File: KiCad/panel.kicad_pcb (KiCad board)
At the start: 2 copper layers, 50 x 50 mm, 38 parts, among them J1 Conn_01x05, J5 USB_C_Receptacle_USB2.0_16P, J6 Conn_01x03, J7 VDD, J8 GND, J9 Conn_01x14, Q1 IRLZ44N, Q2 IRLZ44N, Q3 IRLZ44N, Q4 IRLZ44N, SW1 BOOT, SW2 ENABLE, U1 TPS62132, U2 ESP32-S3-WROOM-2

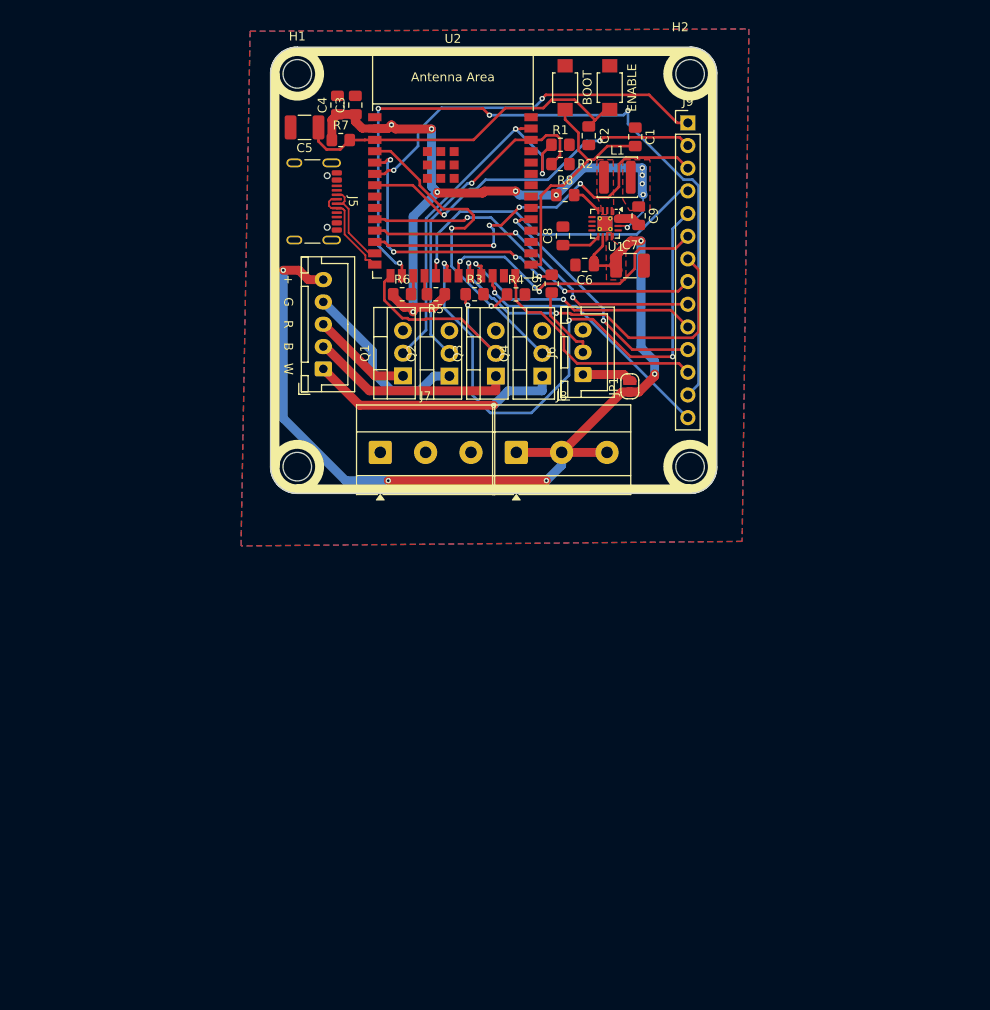
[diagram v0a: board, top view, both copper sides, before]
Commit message: convert to 4 layer pcb
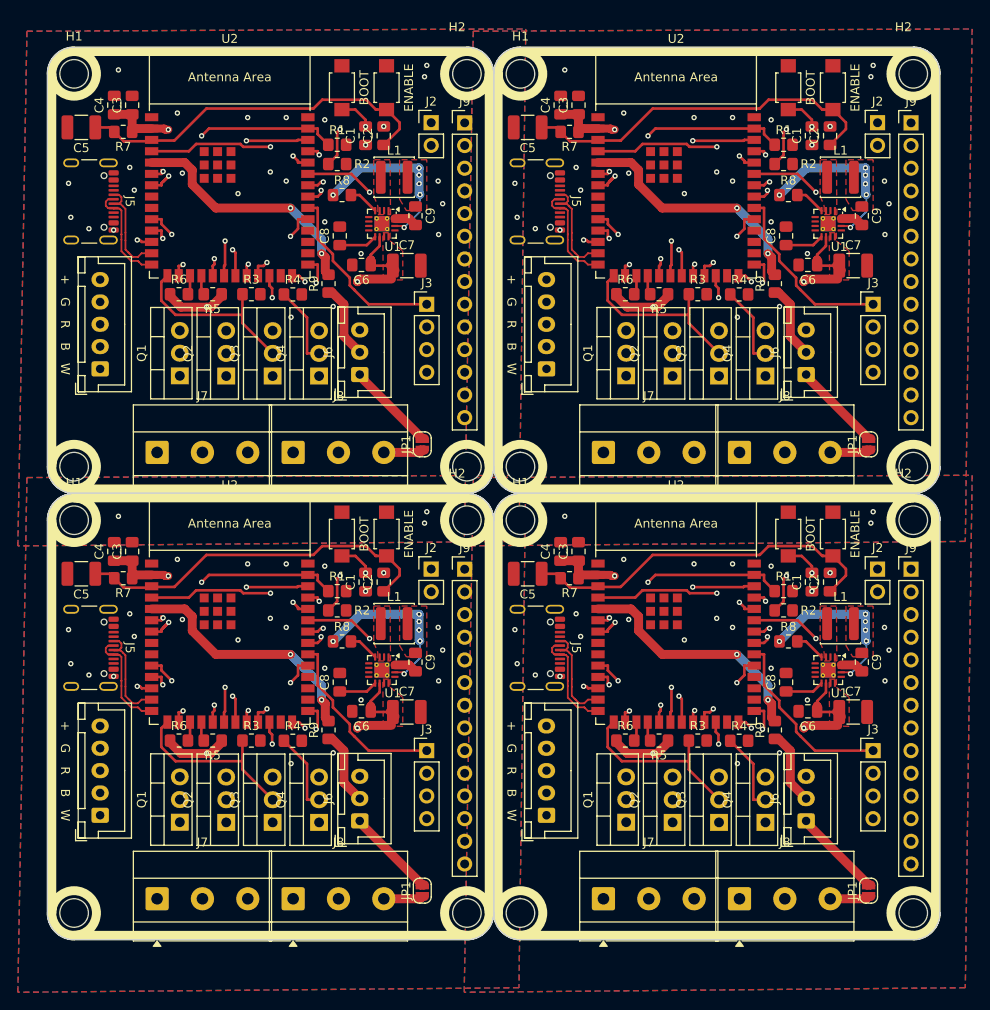
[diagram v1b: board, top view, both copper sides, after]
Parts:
- removed the C1 at (164.4, 30.1)
- removed the C2 at (159.2, 29.9)
- removed the C3 at (133.0, 26.5)
- removed the C4 at (131.0, 26.5)
- removed the C5 at (127.3, 29.0)
- removed the C6 at (158.7, 44.4)
- removed the C7 at (163.8, 44.5)
- removed the C8 at (156.3, 41.1)
- removed the C9 at (164.7, 38.9)
- removed the H1 at (126.5, 23.0)
- removed the H2 at (170.5, 23.0)
- removed the H3 at (170.5, 67.0)
- removed the H4 at (126.5, 67.0)
- removed the J1 at (129.4, 56.0)
- removed the J5 at (127.2, 37.3)
- removed the J6 at (158.5, 56.7)
- removed the J7 at (135.8, 65.4)
- removed the J8 at (151.0, 65.4)
- removed the J9 at (170.2, 28.5)
- removed the JP1 at (163.8, 58.0)
- removed the L1 at (162.4, 34.6)
- removed the Q1 at (138.3, 56.8)
- removed the Q2 at (143.5, 56.9)
- removed the Q3 at (148.7, 56.9)
- removed the Q4 at (153.9, 56.9)
- removed the R1 at (156.0, 30.9)
- removed the R2 at (156.0, 33.1)
- removed the R3 at (146.4, 47.7)
- removed the R4 at (151.0, 47.7)
- removed the R5 at (142.0, 47.7)
- removed the R6 at (138.2, 47.7)
- removed the R7 at (131.4, 30.4)
- removed the R8 at (156.5, 36.6)
- removed the R9 at (155.0, 46.5)
- removed the SW1 at (156.5, 24.6)
- removed the SW2 at (161.5, 24.6)
- removed the U1 at (161.0, 39.8)
- removed the U2 at (143.9, 36.1)
- added C1: 100n, Capacitor_SMD:C_0805_2012Metric_Pad1.18x1.45mm_HandSolder, F.Cu at (184.2, 29.9)
- added C1: 100n, Capacitor_SMD:C_0805_2012Metric_Pad1.18x1.45mm_HandSolder, F.Cu at (134.2, 29.9)
- added C1: 100n, Capacitor_SMD:C_0805_2012Metric_Pad1.18x1.45mm_HandSolder, F.Cu at (134.2, 79.9)
- added C1: 100n, Capacitor_SMD:C_0805_2012Metric_Pad1.18x1.45mm_HandSolder, F.Cu at (184.2, 79.9)
- added C2: 100n, Capacitor_SMD:C_0805_2012Metric_Pad1.18x1.45mm_HandSolder, F.Cu at (136.2, 79.9)
- added C2: 100n, Capacitor_SMD:C_0805_2012Metric_Pad1.18x1.45mm_HandSolder, F.Cu at (136.2, 29.9)
- added C2: 100n, Capacitor_SMD:C_0805_2012Metric_Pad1.18x1.45mm_HandSolder, F.Cu at (186.2, 79.9)
- added C2: 100n, Capacitor_SMD:C_0805_2012Metric_Pad1.18x1.45mm_HandSolder, F.Cu at (186.2, 29.9)
- added C3: 100n, Capacitor_SMD:C_0805_2012Metric_Pad1.18x1.45mm_HandSolder, F.Cu at (108.0, 76.5)
- added C3: 100n, Capacitor_SMD:C_0805_2012Metric_Pad1.18x1.45mm_HandSolder, F.Cu at (158.0, 76.5)
- added C3: 100n, Capacitor_SMD:C_0805_2012Metric_Pad1.18x1.45mm_HandSolder, F.Cu at (108.0, 26.5)
- added C3: 100n, Capacitor_SMD:C_0805_2012Metric_Pad1.18x1.45mm_HandSolder, F.Cu at (158.0, 26.5)
- added C4: 22u, Capacitor_SMD:C_0805_2012Metric_Pad1.18x1.45mm_HandSolder, F.Cu at (156.0, 76.5)
- added C4: 22u, Capacitor_SMD:C_0805_2012Metric_Pad1.18x1.45mm_HandSolder, F.Cu at (156.0, 26.5)
- added C4: 22u, Capacitor_SMD:C_0805_2012Metric_Pad1.18x1.45mm_HandSolder, F.Cu at (106.0, 26.5)
- added C4: 22u, Capacitor_SMD:C_0805_2012Metric_Pad1.18x1.45mm_HandSolder, F.Cu at (106.0, 76.5)
- added C5: 10u, Capacitor_SMD:C_1210_3225Metric_Pad1.33x2.70mm_HandSolder, F.Cu at (152.3, 29.0)
- added C5: 10u, Capacitor_SMD:C_1210_3225Metric_Pad1.33x2.70mm_HandSolder, F.Cu at (102.3, 29.0)
- added C5: 10u, Capacitor_SMD:C_1210_3225Metric_Pad1.33x2.70mm_HandSolder, F.Cu at (102.3, 79.0)
- added C5: 10u, Capacitor_SMD:C_1210_3225Metric_Pad1.33x2.70mm_HandSolder, F.Cu at (152.3, 79.0)
- added C6: 100n, Capacitor_SMD:C_0805_2012Metric_Pad1.18x1.45mm_HandSolder, F.Cu at (183.7, 44.4)
- added C6: 100n, Capacitor_SMD:C_0805_2012Metric_Pad1.18x1.45mm_HandSolder, F.Cu at (133.7, 94.4)
- added C6: 100n, Capacitor_SMD:C_0805_2012Metric_Pad1.18x1.45mm_HandSolder, F.Cu at (183.7, 94.4)
- added C6: 100n, Capacitor_SMD:C_0805_2012Metric_Pad1.18x1.45mm_HandSolder, F.Cu at (133.7, 44.4)
- added C7: 10u, Capacitor_SMD:C_1210_3225Metric_Pad1.33x2.70mm_HandSolder, F.Cu at (138.8, 94.5)
- added C7: 10u, Capacitor_SMD:C_1210_3225Metric_Pad1.33x2.70mm_HandSolder, F.Cu at (188.8, 94.5)
- added C7: 10u, Capacitor_SMD:C_1210_3225Metric_Pad1.33x2.70mm_HandSolder, F.Cu at (188.8, 44.5)
- added C7: 10u, Capacitor_SMD:C_1210_3225Metric_Pad1.33x2.70mm_HandSolder, F.Cu at (138.8, 44.5)
- added C8: 3.3n, Capacitor_SMD:C_0805_2012Metric_Pad1.18x1.45mm_HandSolder, F.Cu at (131.3, 91.1)
- added C8: 3.3n, Capacitor_SMD:C_0805_2012Metric_Pad1.18x1.45mm_HandSolder, F.Cu at (181.3, 41.1)
- added C8: 3.3n, Capacitor_SMD:C_0805_2012Metric_Pad1.18x1.45mm_HandSolder, F.Cu at (181.3, 91.1)
- added C8: 3.3n, Capacitor_SMD:C_0805_2012Metric_Pad1.18x1.45mm_HandSolder, F.Cu at (131.3, 41.1)
- added C9: 22u, Capacitor_SMD:C_0805_2012Metric_Pad1.18x1.45mm_HandSolder, F.Cu at (189.7, 38.9)
- added C9: 22u, Capacitor_SMD:C_0805_2012Metric_Pad1.18x1.45mm_HandSolder, F.Cu at (139.7, 88.9)
- added C9: 22u, Capacitor_SMD:C_0805_2012Metric_Pad1.18x1.45mm_HandSolder, F.Cu at (189.7, 88.9)
- added C9: 22u, Capacitor_SMD:C_0805_2012Metric_Pad1.18x1.45mm_HandSolder, F.Cu at (139.7, 38.9)
- added H1: MountingHole, MountingHole:MountingHole_3.2mm_M3, F.Cu at (151.5, 23.0)
- added H1: MountingHole, MountingHole:MountingHole_3.2mm_M3, F.Cu at (101.5, 23.0)
- added H1: MountingHole, MountingHole:MountingHole_3.2mm_M3, F.Cu at (101.5, 73.0)
- added H1: MountingHole, MountingHole:MountingHole_3.2mm_M3, F.Cu at (151.5, 73.0)
- added H2: MountingHole, MountingHole:MountingHole_3.2mm_M3, F.Cu at (145.5, 23.0)
- added H2: MountingHole, MountingHole:MountingHole_3.2mm_M3, F.Cu at (195.5, 23.0)
- added H2: MountingHole, MountingHole:MountingHole_3.2mm_M3, F.Cu at (195.5, 73.0)
- added H2: MountingHole, MountingHole:MountingHole_3.2mm_M3, F.Cu at (145.5, 73.0)
- added H3: MountingHole, MountingHole:MountingHole_3.2mm_M3, F.Cu at (145.5, 117.0)
- added H3: MountingHole, MountingHole:MountingHole_3.2mm_M3, F.Cu at (195.5, 67.0)
- added H3: MountingHole, MountingHole:MountingHole_3.2mm_M3, F.Cu at (195.5, 117.0)
- added H3: MountingHole, MountingHole:MountingHole_3.2mm_M3, F.Cu at (145.5, 67.0)
- added H4: MountingHole, MountingHole:MountingHole_3.2mm_M3, F.Cu at (101.5, 117.0)
- added H4: MountingHole, MountingHole:MountingHole_3.2mm_M3, F.Cu at (101.5, 67.0)
- added H4: MountingHole, MountingHole:MountingHole_3.2mm_M3, F.Cu at (151.5, 67.0)
- added H4: MountingHole, MountingHole:MountingHole_3.2mm_M3, F.Cu at (151.5, 117.0)
- added J1: Conn_01x05, Connector_JST:JST_XH_B5B-XH-A_1x05_P2.50mm_Vertical, F.Cu at (104.4, 106.0)
- added J1: Conn_01x05, Connector_JST:JST_XH_B5B-XH-A_1x05_P2.50mm_Vertical, F.Cu at (154.4, 106.0)
- added J1: Conn_01x05, Connector_JST:JST_XH_B5B-XH-A_1x05_P2.50mm_Vertical, F.Cu at (154.4, 56.0)
- added J1: Conn_01x05, Connector_JST:JST_XH_B5B-XH-A_1x05_P2.50mm_Vertical, F.Cu at (104.4, 56.0)
- added J2: UART, Connector_PinHeader_2.54mm:PinHeader_1x02_P2.54mm_Vertical, F.Cu at (191.5, 78.5)
- added J2: UART, Connector_PinHeader_2.54mm:PinHeader_1x02_P2.54mm_Vertical, F.Cu at (141.5, 28.5)
- added J2: UART, Connector_PinHeader_2.54mm:PinHeader_1x02_P2.54mm_Vertical, F.Cu at (191.5, 28.5)
- added J2: UART, Connector_PinHeader_2.54mm:PinHeader_1x02_P2.54mm_Vertical, F.Cu at (141.5, 78.5)
- added J3: JTAG, Connector_PinHeader_2.54mm:PinHeader_1x04_P2.54mm_Vertical, F.Cu at (141.0, 48.8)
- added J3: JTAG, Connector_PinHeader_2.54mm:PinHeader_1x04_P2.54mm_Vertical, F.Cu at (191.0, 48.8)
- added J3: JTAG, Connector_PinHeader_2.54mm:PinHeader_1x04_P2.54mm_Vertical, F.Cu at (191.0, 98.8)
- added J3: JTAG, Connector_PinHeader_2.54mm:PinHeader_1x04_P2.54mm_Vertical, F.Cu at (141.0, 98.8)
- added J5: USB_C_Receptacle_USB2.0_16P, Connector_USB:USB_C_Receptacle_GCT_USB4105-xx-A_16P_TopMnt_Horizontal, F.Cu at (102.2, 37.3)
- added J5: USB_C_Receptacle_USB2.0_16P, Connector_USB:USB_C_Receptacle_GCT_USB4105-xx-A_16P_TopMnt_Horizontal, F.Cu at (152.2, 37.3)
- added J5: USB_C_Receptacle_USB2.0_16P, Connector_USB:USB_C_Receptacle_GCT_USB4105-xx-A_16P_TopMnt_Horizontal, F.Cu at (152.2, 87.3)
- added J5: USB_C_Receptacle_USB2.0_16P, Connector_USB:USB_C_Receptacle_GCT_USB4105-xx-A_16P_TopMnt_Horizontal, F.Cu at (102.2, 87.3)
- added J6: Conn_01x03, Connector_JST:JST_XH_B3B-XH-A_1x03_P2.50mm_Vertical, F.Cu at (183.5, 106.7)
- added J6: Conn_01x03, Connector_JST:JST_XH_B3B-XH-A_1x03_P2.50mm_Vertical, F.Cu at (183.5, 56.7)
- added J6: Conn_01x03, Connector_JST:JST_XH_B3B-XH-A_1x03_P2.50mm_Vertical, F.Cu at (133.5, 106.7)
- added J6: Conn_01x03, Connector_JST:JST_XH_B3B-XH-A_1x03_P2.50mm_Vertical, F.Cu at (133.5, 56.7)
- added J7: VDD, TerminalBlock_Phoenix:TerminalBlock_Phoenix_MKDS-1,5-3-5.08_1x03_P5.08mm_Horizontal, F.Cu at (160.8, 115.4)
- added J7: VDD, TerminalBlock_Phoenix:TerminalBlock_Phoenix_MKDS-1,5-3-5.08_1x03_P5.08mm_Horizontal, F.Cu at (160.8, 65.4)
- added J7: VDD, TerminalBlock_Phoenix:TerminalBlock_Phoenix_MKDS-1,5-3-5.08_1x03_P5.08mm_Horizontal, F.Cu at (110.8, 115.4)
- added J7: VDD, TerminalBlock_Phoenix:TerminalBlock_Phoenix_MKDS-1,5-3-5.08_1x03_P5.08mm_Horizontal, F.Cu at (110.8, 65.4)
- added J8: GND, TerminalBlock_Phoenix:TerminalBlock_Phoenix_MKDS-1,5-3-5.08_1x03_P5.08mm_Horizontal, F.Cu at (126.0, 65.4)
- added J8: GND, TerminalBlock_Phoenix:TerminalBlock_Phoenix_MKDS-1,5-3-5.08_1x03_P5.08mm_Horizontal, F.Cu at (176.0, 115.4)
- added J8: GND, TerminalBlock_Phoenix:TerminalBlock_Phoenix_MKDS-1,5-3-5.08_1x03_P5.08mm_Horizontal, F.Cu at (126.0, 115.4)
- added J8: GND, TerminalBlock_Phoenix:TerminalBlock_Phoenix_MKDS-1,5-3-5.08_1x03_P5.08mm_Horizontal, F.Cu at (176.0, 65.4)
- added J9: Conn_01x14, Connector_PinHeader_2.54mm:PinHeader_1x14_P2.54mm_Vertical, F.Cu at (145.2, 78.5)
- added J9: Conn_01x14, Connector_PinHeader_2.54mm:PinHeader_1x14_P2.54mm_Vertical, F.Cu at (195.2, 28.5)
- added J9: Conn_01x14, Connector_PinHeader_2.54mm:PinHeader_1x14_P2.54mm_Vertical, F.Cu at (145.2, 28.5)
- added J9: Conn_01x14, Connector_PinHeader_2.54mm:PinHeader_1x14_P2.54mm_Vertical, F.Cu at (195.2, 78.5)
- added JP1: SolderJumper_2_Open, Jumper:SolderJumper-2_P1.3mm_Open_RoundedPad1.0x1.5mm, F.Cu at (190.5, 64.5)
- added JP1: SolderJumper_2_Open, Jumper:SolderJumper-2_P1.3mm_Open_RoundedPad1.0x1.5mm, F.Cu at (140.5, 64.5)
- added JP1: SolderJumper_2_Open, Jumper:SolderJumper-2_P1.3mm_Open_RoundedPad1.0x1.5mm, F.Cu at (140.5, 114.5)
- added JP1: SolderJumper_2_Open, Jumper:SolderJumper-2_P1.3mm_Open_RoundedPad1.0x1.5mm, F.Cu at (190.5, 114.5)
- added L1: 1/2.2u, Inductor_SMD:L_APV_ANR4026, F.Cu at (187.4, 84.6)
- added L1: 1/2.2u, Inductor_SMD:L_APV_ANR4026, F.Cu at (137.4, 84.6)
- added L1: 1/2.2u, Inductor_SMD:L_APV_ANR4026, F.Cu at (187.4, 34.6)
- added L1: 1/2.2u, Inductor_SMD:L_APV_ANR4026, F.Cu at (137.4, 34.6)
- added Q1: IRLZ44N, Package_TO_SOT_THT:TO-220-3_Vertical, F.Cu at (113.3, 106.8)
- added Q1: IRLZ44N, Package_TO_SOT_THT:TO-220-3_Vertical, F.Cu at (163.3, 106.8)
- added Q1: IRLZ44N, Package_TO_SOT_THT:TO-220-3_Vertical, F.Cu at (163.3, 56.8)
- added Q1: IRLZ44N, Package_TO_SOT_THT:TO-220-3_Vertical, F.Cu at (113.3, 56.8)
- added Q2: IRLZ44N, Package_TO_SOT_THT:TO-220-3_Vertical, F.Cu at (118.5, 106.9)
- added Q2: IRLZ44N, Package_TO_SOT_THT:TO-220-3_Vertical, F.Cu at (168.5, 56.9)
- added Q2: IRLZ44N, Package_TO_SOT_THT:TO-220-3_Vertical, F.Cu at (118.5, 56.9)
- added Q2: IRLZ44N, Package_TO_SOT_THT:TO-220-3_Vertical, F.Cu at (168.5, 106.9)
- added Q3: IRLZ44N, Package_TO_SOT_THT:TO-220-3_Vertical, F.Cu at (173.7, 56.9)
- added Q3: IRLZ44N, Package_TO_SOT_THT:TO-220-3_Vertical, F.Cu at (123.7, 56.9)
- added Q3: IRLZ44N, Package_TO_SOT_THT:TO-220-3_Vertical, F.Cu at (173.7, 106.9)
- added Q3: IRLZ44N, Package_TO_SOT_THT:TO-220-3_Vertical, F.Cu at (123.7, 106.9)
- added Q4: IRLZ44N, Package_TO_SOT_THT:TO-220-3_Vertical, F.Cu at (178.9, 106.9)
- added Q4: IRLZ44N, Package_TO_SOT_THT:TO-220-3_Vertical, F.Cu at (128.9, 56.9)
- added Q4: IRLZ44N, Package_TO_SOT_THT:TO-220-3_Vertical, F.Cu at (178.9, 56.9)
- added Q4: IRLZ44N, Package_TO_SOT_THT:TO-220-3_Vertical, F.Cu at (128.9, 106.9)
- added R1: 100k, Resistor_SMD:R_0805_2012Metric_Pad1.20x1.40mm_HandSolder, F.Cu at (181.0, 30.9)
- added R1: 100k, Resistor_SMD:R_0805_2012Metric_Pad1.20x1.40mm_HandSolder, F.Cu at (131.0, 30.9)
- added R1: 100k, Resistor_SMD:R_0805_2012Metric_Pad1.20x1.40mm_HandSolder, F.Cu at (131.0, 80.9)
- added R1: 100k, Resistor_SMD:R_0805_2012Metric_Pad1.20x1.40mm_HandSolder, F.Cu at (181.0, 80.9)
- added R2: 100k, Resistor_SMD:R_0805_2012Metric_Pad1.20x1.40mm_HandSolder, F.Cu at (181.0, 33.1)
- added R2: 100k, Resistor_SMD:R_0805_2012Metric_Pad1.20x1.40mm_HandSolder, F.Cu at (131.0, 83.1)
- added R2: 100k, Resistor_SMD:R_0805_2012Metric_Pad1.20x1.40mm_HandSolder, F.Cu at (131.0, 33.1)
- added R2: 100k, Resistor_SMD:R_0805_2012Metric_Pad1.20x1.40mm_HandSolder, F.Cu at (181.0, 83.1)
- added R3: 100k, Resistor_SMD:R_0805_2012Metric_Pad1.20x1.40mm_HandSolder, F.Cu at (121.4, 97.7)
- added R3: 100k, Resistor_SMD:R_0805_2012Metric_Pad1.20x1.40mm_HandSolder, F.Cu at (171.4, 97.7)
- added R3: 100k, Resistor_SMD:R_0805_2012Metric_Pad1.20x1.40mm_HandSolder, F.Cu at (121.4, 47.7)
- added R3: 100k, Resistor_SMD:R_0805_2012Metric_Pad1.20x1.40mm_HandSolder, F.Cu at (171.4, 47.7)
- added R4: 100k, Resistor_SMD:R_0805_2012Metric_Pad1.20x1.40mm_HandSolder, F.Cu at (126.0, 97.7)
- added R4: 100k, Resistor_SMD:R_0805_2012Metric_Pad1.20x1.40mm_HandSolder, F.Cu at (176.0, 97.7)
- added R4: 100k, Resistor_SMD:R_0805_2012Metric_Pad1.20x1.40mm_HandSolder, F.Cu at (126.0, 47.7)
- added R4: 100k, Resistor_SMD:R_0805_2012Metric_Pad1.20x1.40mm_HandSolder, F.Cu at (176.0, 47.7)
- added R5: 10k, Resistor_SMD:R_0805_2012Metric_Pad1.20x1.40mm_HandSolder, F.Cu at (117.0, 97.7)
- added R5: 10k, Resistor_SMD:R_0805_2012Metric_Pad1.20x1.40mm_HandSolder, F.Cu at (167.0, 97.7)
- added R5: 10k, Resistor_SMD:R_0805_2012Metric_Pad1.20x1.40mm_HandSolder, F.Cu at (167.0, 47.7)
- added R5: 10k, Resistor_SMD:R_0805_2012Metric_Pad1.20x1.40mm_HandSolder, F.Cu at (117.0, 47.7)
- added R6: 10k, Resistor_SMD:R_0805_2012Metric_Pad1.20x1.40mm_HandSolder, F.Cu at (163.2, 47.7)
- added R6: 10k, Resistor_SMD:R_0805_2012Metric_Pad1.20x1.40mm_HandSolder, F.Cu at (113.2, 97.7)
- added R6: 10k, Resistor_SMD:R_0805_2012Metric_Pad1.20x1.40mm_HandSolder, F.Cu at (163.2, 97.7)
- added R6: 10k, Resistor_SMD:R_0805_2012Metric_Pad1.20x1.40mm_HandSolder, F.Cu at (113.2, 47.7)
- added R7: 10k, Resistor_SMD:R_0805_2012Metric_Pad1.20x1.40mm_HandSolder, F.Cu at (107.0, 29.5)
- added R7: 10k, Resistor_SMD:R_0805_2012Metric_Pad1.20x1.40mm_HandSolder, F.Cu at (107.0, 79.5)
- added R7: 10k, Resistor_SMD:R_0805_2012Metric_Pad1.20x1.40mm_HandSolder, F.Cu at (157.0, 29.5)
- added R7: 10k, Resistor_SMD:R_0805_2012Metric_Pad1.20x1.40mm_HandSolder, F.Cu at (157.0, 79.5)
- added R8: 100k, Resistor_SMD:R_0805_2012Metric_Pad1.20x1.40mm_HandSolder, F.Cu at (131.5, 36.6)
- added R8: 100k, Resistor_SMD:R_0805_2012Metric_Pad1.20x1.40mm_HandSolder, F.Cu at (181.5, 36.6)
- added R8: 100k, Resistor_SMD:R_0805_2012Metric_Pad1.20x1.40mm_HandSolder, F.Cu at (181.5, 86.6)
- added R8: 100k, Resistor_SMD:R_0805_2012Metric_Pad1.20x1.40mm_HandSolder, F.Cu at (131.5, 86.6)
- added R9: 100, Resistor_SMD:R_0805_2012Metric_Pad1.20x1.40mm_HandSolder, F.Cu at (180.0, 46.5)
- added R9: 100, Resistor_SMD:R_0805_2012Metric_Pad1.20x1.40mm_HandSolder, F.Cu at (180.0, 96.5)
- added R9: 100, Resistor_SMD:R_0805_2012Metric_Pad1.20x1.40mm_HandSolder, F.Cu at (130.0, 46.5)
- added R9: 100, Resistor_SMD:R_0805_2012Metric_Pad1.20x1.40mm_HandSolder, F.Cu at (130.0, 96.5)
- added SW1: BOOT, Library:SHOU HAN TS342A2P-WZ, F.Cu at (131.5, 24.6)
- added SW1: BOOT, Library:SHOU HAN TS342A2P-WZ, F.Cu at (131.5, 74.5)
- added SW1: BOOT, Library:SHOU HAN TS342A2P-WZ, F.Cu at (181.5, 74.5)
- added SW1: BOOT, Library:SHOU HAN TS342A2P-WZ, F.Cu at (181.5, 24.6)
- added SW2: ENABLE, Library:SHOU HAN TS342A2P-WZ, F.Cu at (136.5, 24.6)
- added SW2: ENABLE, Library:SHOU HAN TS342A2P-WZ, F.Cu at (136.5, 74.5)
- added SW2: ENABLE, Library:SHOU HAN TS342A2P-WZ, F.Cu at (186.5, 74.5)
- added SW2: ENABLE, Library:SHOU HAN TS342A2P-WZ, F.Cu at (186.5, 24.6)
- added U1: TPS62132, Package_DFN_QFN:VQFN-16-1EP_3x3mm_P0.5mm_EP1.68x1.68mm_ThermalVias, F.Cu at (136.0, 89.8)
- added U1: TPS62132, Package_DFN_QFN:VQFN-16-1EP_3x3mm_P0.5mm_EP1.68x1.68mm_ThermalVias, F.Cu at (186.0, 39.8)
- added U1: TPS62132, Package_DFN_QFN:VQFN-16-1EP_3x3mm_P0.5mm_EP1.68x1.68mm_ThermalVias, F.Cu at (136.0, 39.8)
- added U1: TPS62132, Package_DFN_QFN:VQFN-16-1EP_3x3mm_P0.5mm_EP1.68x1.68mm_ThermalVias, F.Cu at (186.0, 89.8)
- added U2: ESP32-S3-WROOM-2, PCM_Espressif:ESP32-S3-WROOM-2, F.Cu at (118.9, 36.1)
- added U2: ESP32-S3-WROOM-2, PCM_Espressif:ESP32-S3-WROOM-2, F.Cu at (118.9, 86.1)
- added U2: ESP32-S3-WROOM-2, PCM_Espressif:ESP32-S3-WROOM-2, F.Cu at (168.9, 86.1)
- added U2: ESP32-S3-WROOM-2, PCM_Espressif:ESP32-S3-WROOM-2, F.Cu at (168.9, 36.1)
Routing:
- net Board_3-+24V: track 0.00 -> 73.7 mm, vias 0 -> 3
- net Board_2-+24V: track 0.00 -> 73.7 mm, vias 0 -> 3
- net Board_1-+24V: track 0.00 -> 73.7 mm, vias 0 -> 3
- net Board_1-+3.3V: track 0.00 -> 73.3 mm, vias 0 -> 10
- net Board_3-+3.3V: track 0.00 -> 73.3 mm, vias 0 -> 10
- net Board_2-+3.3V: track 0.00 -> 73.3 mm, vias 0 -> 10
- net Board_3-W: track 0.00 -> 48.2 mm, vias 0 -> 1
- net Board_2-W: track 0.00 -> 48.2 mm, vias 0 -> 1
- net Board_1-W: track 0.00 -> 48.2 mm, vias 0 -> 1
- net Board_3-G: track 0.00 -> 47.9 mm, vias 0 -> 2
- net Board_1-G: track 0.00 -> 47.9 mm, vias 0 -> 2
- net Board_2-G: track 0.00 -> 47.9 mm, vias 0 -> 2
- net Board_2-GPIO.11: track 0.00 -> 46.4 mm, vias 0 -> 1
- net Board_1-GPIO.11: track 0.00 -> 46.4 mm, vias 0 -> 1
- net Board_3-GPIO.11: track 0.00 -> 46.4 mm, vias 0 -> 1
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- added copper zone on F.Cu, net Board_1-+24V
- added copper zone on F.Cu, net Board_1-+3.3V
- added copper zone on F.Cu, net Board_1-/3.3V Switch
- added copper zone on B.Cu, net Board_1-GND
- added copper zone on F.Cu, net Board_1-GND
- added copper zone on F.Cu, net Board_2-+24V
- added copper zone on F.Cu, net Board_2-+3.3V
- added copper zone on F.Cu, net Board_2-/3.3V Switch
- added copper zone on B.Cu, net Board_2-GND
- added copper zone on F.Cu, net Board_2-GND
- added copper zone on F.Cu, net Board_3-+24V
- added copper zone on F.Cu, net Board_3-+3.3V
- added copper zone on F.Cu, net Board_3-/3.3V Switch
- added copper zone on B.Cu, net Board_3-GND
- added copper zone on F.Cu, net Board_3-GND
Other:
- board size 50 x 50 mm -> 100 x 100 mm
- copper layers 2 -> 4
- board text added: "V-CUT"

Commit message: jlcpcb order
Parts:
- removed the C1 at (184.2, 29.9)
- removed the C1 at (134.2, 29.9)
- removed the C1 at (134.2, 79.9)
- removed the C1 at (184.2, 79.9)
- removed the C2 at (136.2, 79.9)
- removed the C2 at (136.2, 29.9)
- removed the C2 at (186.2, 79.9)
- removed the C2 at (186.2, 29.9)
- removed the C3 at (108.0, 76.5)
- removed the C3 at (158.0, 76.5)
- removed the C3 at (108.0, 26.5)
- removed the C3 at (158.0, 26.5)
- removed the C4 at (156.0, 76.5)
- removed the C4 at (156.0, 26.5)
- removed the C4 at (106.0, 26.5)
- removed the C4 at (106.0, 76.5)
- removed the C5 at (152.3, 29.0)
- removed the C5 at (102.3, 29.0)
- removed the C5 at (102.3, 79.0)
- removed the C5 at (152.3, 79.0)
- removed the C6 at (183.7, 44.4)
- removed the C6 at (133.7, 94.4)
- removed the C6 at (183.7, 94.4)
- removed the C6 at (133.7, 44.4)
- removed the C7 at (138.8, 94.5)
- removed the C7 at (188.8, 94.5)
- removed the C7 at (188.8, 44.5)
- removed the C7 at (138.8, 44.5)
- removed the C8 at (131.3, 91.1)
- removed the C8 at (181.3, 41.1)
- removed the C8 at (181.3, 91.1)
- removed the C8 at (131.3, 41.1)
- removed the C9 at (189.7, 38.9)
- removed the C9 at (139.7, 88.9)
- removed the C9 at (189.7, 88.9)
- removed the C9 at (139.7, 38.9)
- removed the J1 at (104.4, 106.0)
- removed the J1 at (154.4, 106.0)
- removed the J1 at (154.4, 56.0)
- removed the J1 at (104.4, 56.0)
- removed the J2 at (191.5, 78.5)
- removed the J2 at (141.5, 28.5)
- removed the J2 at (191.5, 28.5)
- removed the J2 at (141.5, 78.5)
- removed the J3 at (141.0, 48.8)
- removed the J3 at (191.0, 48.8)
- removed the J3 at (191.0, 98.8)
- removed the J3 at (141.0, 98.8)
- removed the J5 at (102.2, 37.3)
- removed the J5 at (152.2, 37.3)
- removed the J5 at (152.2, 87.3)
- removed the J5 at (102.2, 87.3)
- removed the J6 at (183.5, 106.7)
- removed the J6 at (183.5, 56.7)
- removed the J6 at (133.5, 106.7)
- removed the J6 at (133.5, 56.7)
- removed the J7 at (160.8, 115.4)
- removed the J7 at (160.8, 65.4)
- removed the J7 at (110.8, 115.4)
- removed the J7 at (110.8, 65.4)
- removed the J8 at (126.0, 65.4)
- removed the J8 at (176.0, 115.4)
- removed the J8 at (126.0, 115.4)
- removed the J8 at (176.0, 65.4)
- removed J9 (x4): Conn_01x14, Connector_PinHeader_2.54mm:PinHeader_1x14_P2.54mm_Vertical
- removed the JP1 at (190.5, 64.5)
- removed the JP1 at (140.5, 64.5)
- removed the JP1 at (140.5, 114.5)
- removed the JP1 at (190.5, 114.5)
- removed the L1 at (187.4, 84.6)
- removed the L1 at (137.4, 84.6)
- removed the L1 at (187.4, 34.6)
- removed the L1 at (137.4, 34.6)
- removed the R1 at (181.0, 30.9)
- removed the R1 at (131.0, 30.9)
- removed the R1 at (131.0, 80.9)
- removed the R1 at (181.0, 80.9)
- removed the R2 at (181.0, 33.1)
- removed the R2 at (131.0, 83.1)
- removed the R2 at (131.0, 33.1)
- removed the R2 at (181.0, 83.1)
- removed the R3 at (121.4, 97.7)
- removed the R3 at (171.4, 97.7)
- removed the R3 at (121.4, 47.7)
- removed the R3 at (171.4, 47.7)
- removed the R4 at (126.0, 97.7)
- removed the R4 at (176.0, 97.7)
- removed the R4 at (126.0, 47.7)
- removed the R4 at (176.0, 47.7)
- removed the R5 at (117.0, 97.7)
- removed the R5 at (167.0, 97.7)
- removed the R5 at (167.0, 47.7)
- removed the R5 at (117.0, 47.7)
- removed the R6 at (163.2, 47.7)
- removed the R6 at (113.2, 97.7)
- removed the R6 at (163.2, 97.7)
- removed the R6 at (113.2, 47.7)
- removed the R7 at (107.0, 29.5)
- removed the R7 at (107.0, 79.5)
- removed the R7 at (157.0, 29.5)
- removed the R7 at (157.0, 79.5)
- removed the R8 at (131.5, 36.6)
- removed the R8 at (181.5, 36.6)
- removed the R8 at (181.5, 86.6)
- removed the R8 at (131.5, 86.6)
- removed the R9 at (180.0, 46.5)
- removed the R9 at (180.0, 96.5)
- removed the R9 at (130.0, 46.5)
- removed the R9 at (130.0, 96.5)
- removed the SW1 at (131.5, 24.6)
- removed the SW1 at (131.5, 74.5)
- removed the SW1 at (181.5, 74.5)
- removed the SW1 at (181.5, 24.6)
- removed the SW2 at (136.5, 24.6)
- removed the SW2 at (136.5, 74.5)
- removed the SW2 at (186.5, 74.5)
- removed the SW2 at (186.5, 24.6)
- removed the U1 at (136.0, 89.8)
- removed the U1 at (186.0, 39.8)
- removed the U1 at (136.0, 39.8)
- removed the U1 at (186.0, 89.8)
- removed the U2 at (118.9, 36.1)
- removed the U2 at (118.9, 86.1)
- removed the U2 at (168.9, 86.1)
- removed the U2 at (168.9, 36.1)
- added C1: 100n, Capacitor_SMD:C_0805_2012Metric_Pad1.18x1.45mm_HandSolder, F.Cu at (153.2, 77.6)
- added C1: 100n, Capacitor_SMD:C_0805_2012Metric_Pad1.18x1.45mm_HandSolder, F.Cu at (103.2, 27.6)
- added C1: 100n, Capacitor_SMD:C_0805_2012Metric_Pad1.18x1.45mm_HandSolder, F.Cu at (153.2, 27.6)
- added C1: 100n, Capacitor_SMD:C_0805_2012Metric_Pad1.18x1.45mm_HandSolder, F.Cu at (103.2, 77.6)
- added C10: 10u, Capacitor_SMD:C_0805_2012Metric_Pad1.18x1.45mm_HandSolder, F.Cu at (161.3, 90.3)
- added C10: 10u, Capacitor_SMD:C_0805_2012Metric_Pad1.18x1.45mm_HandSolder, F.Cu at (111.3, 40.3)
- added C10: 10u, Capacitor_SMD:C_0805_2012Metric_Pad1.18x1.45mm_HandSolder, F.Cu at (111.3, 90.3)
- added C10: 10u, Capacitor_SMD:C_0805_2012Metric_Pad1.18x1.45mm_HandSolder, F.Cu at (161.3, 40.3)
- added C11: 10u, Capacitor_SMD:C_0805_2012Metric_Pad1.18x1.45mm_HandSolder, F.Cu at (161.3, 88.3)
- added C11: 10u, Capacitor_SMD:C_0805_2012Metric_Pad1.18x1.45mm_HandSolder, F.Cu at (111.3, 88.3)
- added C11: 10u, Capacitor_SMD:C_0805_2012Metric_Pad1.18x1.45mm_HandSolder, F.Cu at (161.3, 38.3)
- added C11: 10u, Capacitor_SMD:C_0805_2012Metric_Pad1.18x1.45mm_HandSolder, F.Cu at (111.3, 38.3)
- added C12: 10u, Capacitor_SMD:C_0805_2012Metric_Pad1.18x1.45mm_HandSolder, F.Cu at (169.7, 77.1)
- added C12: 10u, Capacitor_SMD:C_0805_2012Metric_Pad1.18x1.45mm_HandSolder, F.Cu at (119.7, 27.1)
- added C12: 10u, Capacitor_SMD:C_0805_2012Metric_Pad1.18x1.45mm_HandSolder, F.Cu at (119.7, 77.1)
- added C12: 10u, Capacitor_SMD:C_0805_2012Metric_Pad1.18x1.45mm_HandSolder, F.Cu at (169.7, 27.1)
- added C2: 100n, Capacitor_SMD:C_0805_2012Metric_Pad1.18x1.45mm_HandSolder, F.Cu at (164.6, 26.5)
- added C2: 100n, Capacitor_SMD:C_0805_2012Metric_Pad1.18x1.45mm_HandSolder, F.Cu at (164.6, 76.5)
- added C2: 100n, Capacitor_SMD:C_0805_2012Metric_Pad1.18x1.45mm_HandSolder, F.Cu at (114.6, 76.5)
- added C2: 100n, Capacitor_SMD:C_0805_2012Metric_Pad1.18x1.45mm_HandSolder, F.Cu at (114.6, 26.5)
- added C3: 100n, Capacitor_SMD:C_0805_2012Metric_Pad1.18x1.45mm_HandSolder, F.Cu at (171.7, 77.1)
- added C3: 100n, Capacitor_SMD:C_0805_2012Metric_Pad1.18x1.45mm_HandSolder, F.Cu at (121.7, 27.1)
- added C3: 100n, Capacitor_SMD:C_0805_2012Metric_Pad1.18x1.45mm_HandSolder, F.Cu at (171.7, 27.1)
- added C3: 100n, Capacitor_SMD:C_0805_2012Metric_Pad1.18x1.45mm_HandSolder, F.Cu at (121.7, 77.1)
- added C4: 10u, Capacitor_SMD:C_0805_2012Metric_Pad1.18x1.45mm_HandSolder, F.Cu at (117.6, 27.1)
- added C4: 10u, Capacitor_SMD:C_0805_2012Metric_Pad1.18x1.45mm_HandSolder, F.Cu at (167.6, 27.1)
- added C4: 10u, Capacitor_SMD:C_0805_2012Metric_Pad1.18x1.45mm_HandSolder, F.Cu at (167.6, 77.1)
- added C4: 10u, Capacitor_SMD:C_0805_2012Metric_Pad1.18x1.45mm_HandSolder, F.Cu at (117.6, 77.1)
- added C5: 10u, Capacitor_SMD:C_0805_2012Metric_Pad1.18x1.45mm_HandSolder, F.Cu at (116.1, 30.2)
- added C5: 10u, Capacitor_SMD:C_0805_2012Metric_Pad1.18x1.45mm_HandSolder, F.Cu at (166.1, 80.2)
- added C5: 10u, Capacitor_SMD:C_0805_2012Metric_Pad1.18x1.45mm_HandSolder, F.Cu at (166.1, 30.2)
- added C5: 10u, Capacitor_SMD:C_0805_2012Metric_Pad1.18x1.45mm_HandSolder, F.Cu at (116.1, 80.2)
- added C6: 100n, Capacitor_SMD:C_0805_2012Metric_Pad1.18x1.45mm_HandSolder, F.Cu at (166.1, 32.2)
- added C6: 100n, Capacitor_SMD:C_0805_2012Metric_Pad1.18x1.45mm_HandSolder, F.Cu at (116.1, 82.2)
- added C6: 100n, Capacitor_SMD:C_0805_2012Metric_Pad1.18x1.45mm_HandSolder, F.Cu at (166.1, 82.2)
- added C6: 100n, Capacitor_SMD:C_0805_2012Metric_Pad1.18x1.45mm_HandSolder, F.Cu at (116.1, 32.2)
- added C7: 100n, Capacitor_SMD:C_0805_2012Metric_Pad1.18x1.45mm_HandSolder, F.Cu at (166.1, 41.6)
- added C7: 100n, Capacitor_SMD:C_0805_2012Metric_Pad1.18x1.45mm_HandSolder, F.Cu at (116.1, 91.6)
- added C7: 100n, Capacitor_SMD:C_0805_2012Metric_Pad1.18x1.45mm_HandSolder, F.Cu at (116.1, 41.6)
- added C7: 100n, Capacitor_SMD:C_0805_2012Metric_Pad1.18x1.45mm_HandSolder, F.Cu at (166.1, 91.6)
- added C8: 10u, Capacitor_SMD:C_0805_2012Metric_Pad1.18x1.45mm_HandSolder, F.Cu at (166.1, 88.6)
- added C8: 10u, Capacitor_SMD:C_0805_2012Metric_Pad1.18x1.45mm_HandSolder, F.Cu at (166.1, 38.6)
- added C8: 10u, Capacitor_SMD:C_0805_2012Metric_Pad1.18x1.45mm_HandSolder, F.Cu at (116.1, 38.6)
- added C8: 10u, Capacitor_SMD:C_0805_2012Metric_Pad1.18x1.45mm_HandSolder, F.Cu at (116.1, 88.6)
- added C9: 10u, Capacitor_SMD:C_0805_2012Metric_Pad1.18x1.45mm_HandSolder, F.Cu at (111.3, 92.4)
- added C9: 10u, Capacitor_SMD:C_0805_2012Metric_Pad1.18x1.45mm_HandSolder, F.Cu at (111.3, 42.4)
- added C9: 10u, Capacitor_SMD:C_0805_2012Metric_Pad1.18x1.45mm_HandSolder, F.Cu at (161.3, 42.4)
- added C9: 10u, Capacitor_SMD:C_0805_2012Metric_Pad1.18x1.45mm_HandSolder, F.Cu at (161.3, 92.4)
- added D1: LED, LED_SMD:LED_0603_1608Metric_Pad1.05x0.95mm_HandSolder, F.Cu at (166.1, 95.3)
- added D1: LED, LED_SMD:LED_0603_1608Metric_Pad1.05x0.95mm_HandSolder, F.Cu at (166.1, 45.3)
- added D1: LED, LED_SMD:LED_0603_1608Metric_Pad1.05x0.95mm_HandSolder, F.Cu at (116.1, 95.3)
- added D1: LED, LED_SMD:LED_0603_1608Metric_Pad1.05x0.95mm_HandSolder, F.Cu at (116.1, 45.3)
- added J1: UART, Connector_PinHeader_2.54mm:PinHeader_1x02_P2.54mm_Vertical, F.Cu at (170.2, 72.3)
- added J1: UART, Connector_PinHeader_2.54mm:PinHeader_1x02_P2.54mm_Vertical, F.Cu at (120.2, 72.3)
- added J1: UART, Connector_PinHeader_2.54mm:PinHeader_1x02_P2.54mm_Vertical, F.Cu at (170.2, 22.3)
- added J1: UART, Connector_PinHeader_2.54mm:PinHeader_1x02_P2.54mm_Vertical, F.Cu at (120.2, 22.3)
- added J2: VDD, TerminalBlock_Phoenix:TerminalBlock_Phoenix_MKDS-1,5-3-5.08_1x03_P5.08mm_Horizontal, F.Cu at (110.8, 115.4)
- added J2: VDD, TerminalBlock_Phoenix:TerminalBlock_Phoenix_MKDS-1,5-3-5.08_1x03_P5.08mm_Horizontal, F.Cu at (160.8, 65.4)
- added J2: VDD, TerminalBlock_Phoenix:TerminalBlock_Phoenix_MKDS-1,5-3-5.08_1x03_P5.08mm_Horizontal, F.Cu at (110.8, 65.4)
- added J2: VDD, TerminalBlock_Phoenix:TerminalBlock_Phoenix_MKDS-1,5-3-5.08_1x03_P5.08mm_Horizontal, F.Cu at (160.8, 115.4)
- added J3: GND, TerminalBlock_Phoenix:TerminalBlock_Phoenix_MKDS-1,5-3-5.08_1x03_P5.08mm_Horizontal, F.Cu at (176.0, 115.4)
- added J3: GND, TerminalBlock_Phoenix:TerminalBlock_Phoenix_MKDS-1,5-3-5.08_1x03_P5.08mm_Horizontal, F.Cu at (126.0, 115.4)
- added J3: GND, TerminalBlock_Phoenix:TerminalBlock_Phoenix_MKDS-1,5-3-5.08_1x03_P5.08mm_Horizontal, F.Cu at (176.0, 65.4)
- added J3: GND, TerminalBlock_Phoenix:TerminalBlock_Phoenix_MKDS-1,5-3-5.08_1x03_P5.08mm_Horizontal, F.Cu at (126.0, 65.4)
- added J4: Conn_01x05, Connector_JST:JST_XH_B5B-XH-A_1x05_P2.50mm_Vertical, F.Cu at (154.4, 57.0)
- added J4: Conn_01x05, Connector_JST:JST_XH_B5B-XH-A_1x05_P2.50mm_Vertical, F.Cu at (154.4, 107.0)
- added J4: Conn_01x05, Connector_JST:JST_XH_B5B-XH-A_1x05_P2.50mm_Vertical, F.Cu at (104.4, 57.0)
- added J4: Conn_01x05, Connector_JST:JST_XH_B5B-XH-A_1x05_P2.50mm_Vertical, F.Cu at (104.4, 107.0)
- added J5: Conn_01x03, Connector_JST:JST_XH_B3B-XH-A_1x03_P2.50mm_Vertical, F.Cu at (183.5, 106.7)
- added J5: Conn_01x03, Connector_JST:JST_XH_B3B-XH-A_1x03_P2.50mm_Vertical, F.Cu at (133.5, 106.7)
- added J5: Conn_01x03, Connector_JST:JST_XH_B3B-XH-A_1x03_P2.50mm_Vertical, F.Cu at (133.5, 56.7)
- added J5: Conn_01x03, Connector_JST:JST_XH_B3B-XH-A_1x03_P2.50mm_Vertical, F.Cu at (183.5, 56.7)
- added J6: USB_C_Receptacle_USB2.0_16P, Connector_USB:USB_C_Receptacle_GCT_USB4105-xx-A_16P_TopMnt_Horizontal, F.Cu at (102.2, 35.1)
- added J6: USB_C_Receptacle_USB2.0_16P, Connector_USB:USB_C_Receptacle_GCT_USB4105-xx-A_16P_TopMnt_Horizontal, F.Cu at (102.2, 85.1)
- added J6: USB_C_Receptacle_USB2.0_16P, Connector_USB:USB_C_Receptacle_GCT_USB4105-xx-A_16P_TopMnt_Horizontal, F.Cu at (152.2, 85.1)
- added J6: USB_C_Receptacle_USB2.0_16P, Connector_USB:USB_C_Receptacle_GCT_USB4105-xx-A_16P_TopMnt_Horizontal, F.Cu at (152.2, 35.1)
- added J7: Conn_01x14, Connector_PinHeader_2.54mm:PinHeader_1x14_P2.54mm_Vertical, F.Cu at (194.1, 78.5)
- added J7: Conn_01x14, Connector_PinHeader_2.54mm:PinHeader_1x14_P2.54mm_Vertical, F.Cu at (144.1, 28.5)
- added J7: Conn_01x14, Connector_PinHeader_2.54mm:PinHeader_1x14_P2.54mm_Vertical, F.Cu at (144.1, 78.5)
- added J7: Conn_01x14, Connector_PinHeader_2.54mm:PinHeader_1x14_P2.54mm_Vertical, F.Cu at (194.1, 28.5)
- added J8: JTAG, Connector_PinHeader_2.54mm:PinHeader_1x04_P2.54mm_Vertical, F.Cu at (141.0, 48.8)
- added J8: JTAG, Connector_PinHeader_2.54mm:PinHeader_1x04_P2.54mm_Vertical, F.Cu at (191.0, 98.8)
- added J8: JTAG, Connector_PinHeader_2.54mm:PinHeader_1x04_P2.54mm_Vertical, F.Cu at (191.0, 48.8)
- added J8: JTAG, Connector_PinHeader_2.54mm:PinHeader_1x04_P2.54mm_Vertical, F.Cu at (141.0, 98.8)
- added JP1: SolderJumper_2_Open, Jumper:SolderJumper-2_P1.3mm_Open_RoundedPad1.0x1.5mm, F.Cu at (140.5, 64.8)
- added JP1: SolderJumper_2_Open, Jumper:SolderJumper-2_P1.3mm_Open_RoundedPad1.0x1.5mm, F.Cu at (140.5, 114.8)
- added JP1: SolderJumper_2_Open, Jumper:SolderJumper-2_P1.3mm_Open_RoundedPad1.0x1.5mm, F.Cu at (190.5, 64.8)
- added JP1: SolderJumper_2_Open, Jumper:SolderJumper-2_P1.3mm_Open_RoundedPad1.0x1.5mm, F.Cu at (190.5, 114.8)
- added L1: 15u, Inductor_SMD:L_APV_ANR4026, F.Cu at (111.3, 35.0)
- added L1: 15u, Inductor_SMD:L_APV_ANR4026, F.Cu at (111.3, 85.0)
- added L1: 15u, Inductor_SMD:L_APV_ANR4026, F.Cu at (161.3, 85.0)
- added L1: 15u, Inductor_SMD:L_APV_ANR4026, F.Cu at (161.3, 35.0)
- added R1: 100k, Resistor_SMD:R_0805_2012Metric_Pad1.20x1.40mm_HandSolder, B.Cu at (111.3, 46.9)
- added R1: 100k, Resistor_SMD:R_0805_2012Metric_Pad1.20x1.40mm_HandSolder, B.Cu at (161.3, 96.9)
- added R1: 100k, Resistor_SMD:R_0805_2012Metric_Pad1.20x1.40mm_HandSolder, B.Cu at (111.3, 96.9)
- added R1: 100k, Resistor_SMD:R_0805_2012Metric_Pad1.20x1.40mm_HandSolder, B.Cu at (161.3, 46.9)
- added R10: 100k, Resistor_SMD:R_0805_2012Metric_Pad1.20x1.40mm_HandSolder, F.Cu at (119.2, 85.0)
- added R10: 100k, Resistor_SMD:R_0805_2012Metric_Pad1.20x1.40mm_HandSolder, F.Cu at (169.2, 85.0)
- added R10: 100k, Resistor_SMD:R_0805_2012Metric_Pad1.20x1.40mm_HandSolder, F.Cu at (119.2, 35.0)
- added R10: 100k, Resistor_SMD:R_0805_2012Metric_Pad1.20x1.40mm_HandSolder, F.Cu at (169.2, 35.0)
- added R11: 1.8k, Resistor_SMD:R_0805_2012Metric_Pad1.20x1.40mm_HandSolder, F.Cu at (120.2, 38.8)
- added R11: 1.8k, Resistor_SMD:R_0805_2012Metric_Pad1.20x1.40mm_HandSolder, F.Cu at (170.2, 38.8)
- added R11: 1.8k, Resistor_SMD:R_0805_2012Metric_Pad1.20x1.40mm_HandSolder, F.Cu at (170.2, 88.8)
- added R11: 1.8k, Resistor_SMD:R_0805_2012Metric_Pad1.20x1.40mm_HandSolder, F.Cu at (120.2, 88.8)
- added R12: 20k, Resistor_SMD:R_0805_2012Metric_Pad1.20x1.40mm_HandSolder, F.Cu at (170.2, 91.6)
- added R12: 20k, Resistor_SMD:R_0805_2012Metric_Pad1.20x1.40mm_HandSolder, F.Cu at (170.2, 41.6)
- added R12: 20k, Resistor_SMD:R_0805_2012Metric_Pad1.20x1.40mm_HandSolder, F.Cu at (120.2, 41.6)
- added R12: 20k, Resistor_SMD:R_0805_2012Metric_Pad1.20x1.40mm_HandSolder, F.Cu at (120.2, 91.6)
- added R2: 100k, Resistor_SMD:R_0805_2012Metric_Pad1.20x1.40mm_HandSolder, B.Cu at (115.9, 96.9)
- added R2: 100k, Resistor_SMD:R_0805_2012Metric_Pad1.20x1.40mm_HandSolder, B.Cu at (115.9, 46.9)
- added R2: 100k, Resistor_SMD:R_0805_2012Metric_Pad1.20x1.40mm_HandSolder, B.Cu at (165.9, 46.9)
- added R2: 100k, Resistor_SMD:R_0805_2012Metric_Pad1.20x1.40mm_HandSolder, B.Cu at (165.9, 96.9)
- added R3: 100k, Resistor_SMD:R_0805_2012Metric_Pad1.20x1.40mm_HandSolder, B.Cu at (120.9, 96.9)
- added R3: 100k, Resistor_SMD:R_0805_2012Metric_Pad1.20x1.40mm_HandSolder, B.Cu at (170.9, 46.9)
- added R3: 100k, Resistor_SMD:R_0805_2012Metric_Pad1.20x1.40mm_HandSolder, B.Cu at (120.9, 46.9)
- added R3: 100k, Resistor_SMD:R_0805_2012Metric_Pad1.20x1.40mm_HandSolder, B.Cu at (170.9, 96.9)
- added R4: 100k, Resistor_SMD:R_0805_2012Metric_Pad1.20x1.40mm_HandSolder, B.Cu at (176.5, 46.9)
- added R4: 100k, Resistor_SMD:R_0805_2012Metric_Pad1.20x1.40mm_HandSolder, B.Cu at (176.5, 96.9)
- added R4: 100k, Resistor_SMD:R_0805_2012Metric_Pad1.20x1.40mm_HandSolder, B.Cu at (126.5, 46.9)
- added R4: 100k, Resistor_SMD:R_0805_2012Metric_Pad1.20x1.40mm_HandSolder, B.Cu at (126.5, 96.9)
- added R5: 10k, Resistor_SMD:R_0805_2012Metric_Pad1.20x1.40mm_HandSolder, B.Cu at (129.3, 92.1)
- added R5: 10k, Resistor_SMD:R_0805_2012Metric_Pad1.20x1.40mm_HandSolder, B.Cu at (179.3, 92.1)
- added R5: 10k, Resistor_SMD:R_0805_2012Metric_Pad1.20x1.40mm_HandSolder, B.Cu at (129.3, 42.1)
- added R5: 10k, Resistor_SMD:R_0805_2012Metric_Pad1.20x1.40mm_HandSolder, B.Cu at (179.3, 42.1)
- added R6: 10k, Resistor_SMD:R_0805_2012Metric_Pad1.20x1.40mm_HandSolder, B.Cu at (127.3, 42.1)
- added R6: 10k, Resistor_SMD:R_0805_2012Metric_Pad1.20x1.40mm_HandSolder, B.Cu at (177.3, 92.1)
- added R6: 10k, Resistor_SMD:R_0805_2012Metric_Pad1.20x1.40mm_HandSolder, B.Cu at (177.3, 42.1)
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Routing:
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- added copper zone on F.Cu, net Board_0-Net-(U1-SW)
- added copper zone on F.Cu, net Board_1-Net-(U1-SW)
- added copper zone on F.Cu, net Board_2-Net-(U1-SW)
- added copper zone on F.Cu, net Board_3-Net-(U1-SW)
- removed copper zone on F.Cu, net Board_0-+24V
- removed copper zone on F.Cu, net Board_0-+3.3V
- removed copper zone on F.Cu, net Board_0-/3.3V Switch
- removed copper zone on F.Cu, net Board_1-+24V
- removed copper zone on F.Cu, net Board_1-+3.3V
- removed copper zone on F.Cu, net Board_1-/3.3V Switch
- removed copper zone on F.Cu, net Board_2-+24V
- removed copper zone on F.Cu, net Board_2-+3.3V
- removed copper zone on F.Cu, net Board_2-/3.3V Switch
- removed copper zone on F.Cu, net Board_3-+24V
- removed copper zone on F.Cu, net Board_3-+3.3V
- removed copper zone on F.Cu, net Board_3-/3.3V Switch
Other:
- board text added: "+5-24V"
- board text added: "3V3"
- board text added: "CK"
- board text added: "DATA"
- board text added: "DI"
- board text added: "DO"
- board text added: "G11"
- board text added: "G12"
- board text added: "G13"
- board text added: "G14"
- board text added: "G17"
- board text added: "G18"
- board text added: "G21"
- board text added: "G38"
- board text added: "G45"
- board text added: "G46"
- board text added: "G47"
- board text added: "G8"
- board text added: "GND"
- board text added: "LED Controller Designed by Paulus Handke 2025-06-02 V1"
- board text added: "MS"
- board text added: "PH"
- board text added: "RX"
- board text added: "TX"
- board text added: "VDD"
